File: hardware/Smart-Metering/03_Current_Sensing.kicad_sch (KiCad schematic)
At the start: 40 parts, among them J301 SENSOR_IA, J302 SENSOR_IB, J303 SENSOR_IC, J304 SENSOR_IN

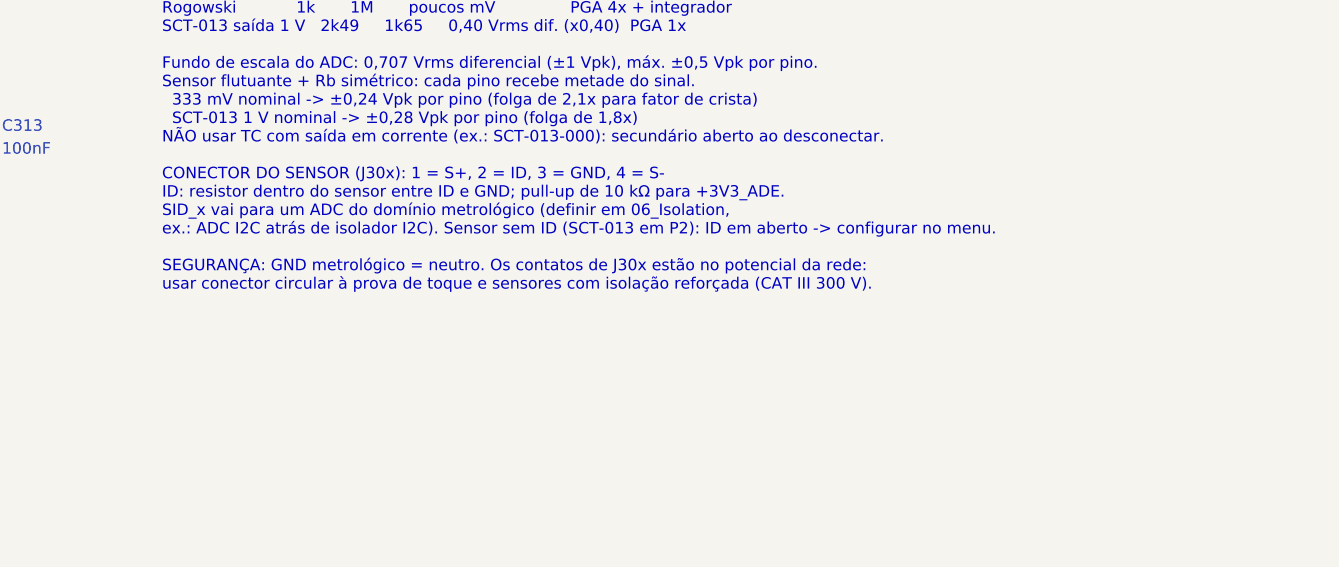
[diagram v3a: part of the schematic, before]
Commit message: Resolve as pendências da revisão do esquemático
P1  ADE9430: footprint VQFN-40 6x6 com EP de 4,15 mm, compatível com as
    variantes CP-40 de 6x6 mm (EP de 3,9 a 4,7 mm).
P2  Confirmado no datasheet: MISO solto com SS alto (pull-up de 100 kΩ)
    e NC1/NC2 em GND, como já estava.
P3  J301-J304: headers JST PH de 4 vias cabeados até conectores M8
    fêmea de painel (à prova de toque).
P4  PS601 -> U606 ADuM6000 (isoPower 5 kVrms, símbolo oficial).
P5  PS101 -> RAC20-05SK/277 (85-305 VAC, 120-430 VDC, 20 W); fusíveis
    T500mA, R101 3 W, C101 10 uF/450 V; entrada do BQ25895 a 3 A.
P7  TPS61089 -> TPS61022 (compensação interna, sem valores a ajustar).
P8  Placa EV alimentada pelos pinos 5 V do J1 (nota na folha 07).
P9  EEPROM de calibração 24LC64 no I2C1.
P10 Labels globais de uma só folha convertidos em locais.

Verificação: 223 componentes, nenhum pino solto, nenhuma net sem fonte,
nenhum conflito de saída, isolação íntegra, todos os footprints
existentes na biblioteca oficial do KiCad.

Co-Authored-By: Claude Opus 5.5 <noreply@anthropic.com>
Claude-Session: https://claude.ai/code/session_012B8cVkhtjf3eg98UdpNCpf
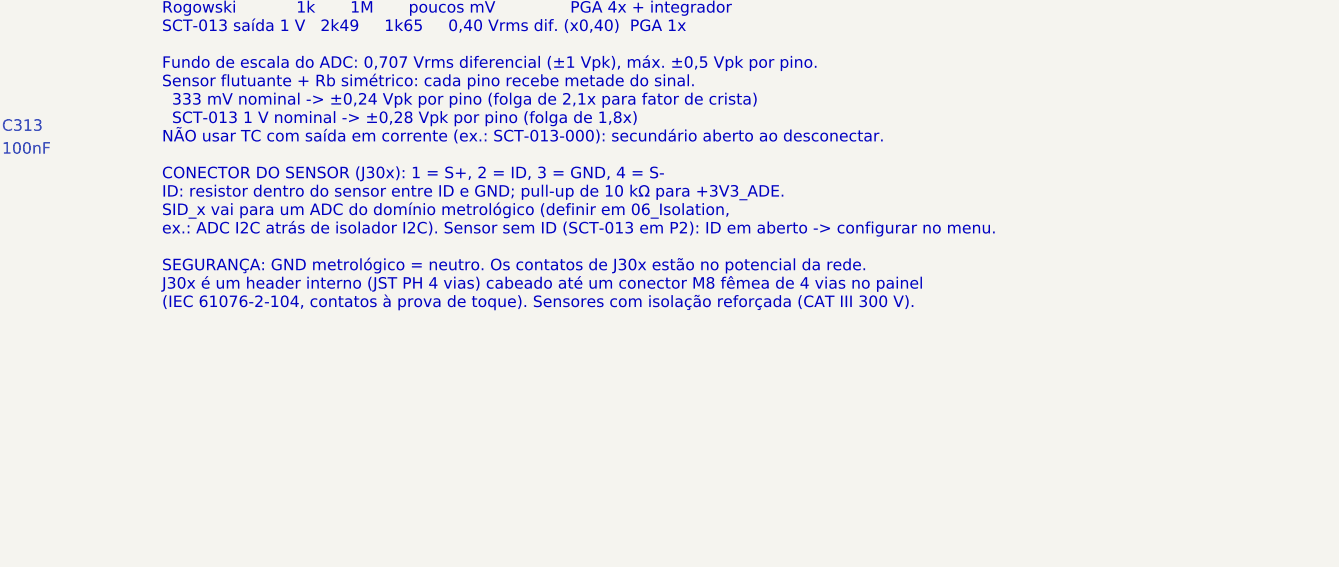
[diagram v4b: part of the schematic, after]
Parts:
- J301, J302, J303, J304: footprint (none) -> Connector_JST:JST_PH_B4B-PH-K_1x04_P2.00mm_Vertical
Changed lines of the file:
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@@
 		(comment 2 "Per leg: Ra series + Rb to GND + 22 nF; Thevenin kept at 1 kOhm for 7.2 kHz anti-aliasing")
 	)
-	(text "FRONT-END DE CORRENTE — ENTRADA CONFIGURÁVEL POR MONTAGEM\n\nPor perna: sensor -> Ra (série) -> nó -> Rb para GND + 22 nF -> IxP / IxN\nRa // Rb = 1 kΩ em todas as opções -> fc ≈ 7,2 kHz (igual aos canais de tensão)\n\nOPÇÃO               Ra       Rb       sinal nominal no ADC    ADE9430\nTC 333 mV (padrão)  1k       1M       0,333 Vrms dif.         PGA 1x\nRogowski            1k       1M       poucos mV               PGA 4x + integrador\nSCT-013 saída 1 V   2k49     1k65     0,40 Vrms dif. (x0,40)  PGA 1x\n\nFundo de escala do ADC: 0,707 Vrms diferencial (±1 Vpk), máx. ±0,5 Vpk por pino.\nSensor flutuante + Rb simétrico: cada pino recebe metade do sinal.\n  333 mV nominal -> ±0,24 Vpk por pino (folga de 2,1x para fator de crista)\n  SCT-013 1 V nominal -> ±0,28 Vpk por pino (folga de 1,8x)\nNÃO usar TC com saída em corrente (ex.: SCT-013-000): secundário aberto ao desconectar.\n\nCONECTOR DO SENSOR (J30x): 1 = S+, 2 = ID, 3 = GND, 4 = S-\nID: resistor dentro do sensor entre ID e GND; pull-up de 10 kΩ para +3V3_ADE.\nSID_x vai para um ADC do domínio metrológico (definir em 06_Isolation,\nex.: ADC I2C atrás de isolador I2C). Sensor sem ID (SCT-013 em P2): ID em aberto -> configurar no menu.\n\nSEGURANÇA: GND metrológico = neutro. Os contatos de J30x estão no potencial da rede:\nusar conector circular à prova de toque e sensores com isolação reforçada (CAT III 300 V)."
+	(text "FRONT-END DE CORRENTE — ENTRADA CONFIGURÁVEL POR MONTAGEM\n\nPor perna: sensor -> Ra (série) -> nó -> Rb para GND + 22 nF -> IxP / IxN\nRa // Rb = 1 kΩ em todas as opções -> fc ≈ 7,2 kHz (igual aos canais de tensão)\n\nOPÇÃO               Ra       Rb       sinal nominal no ADC    ADE9430\nTC 333 mV (padrão)  1k       1M       0,333 Vrms dif.         PGA 1x\nRogowski            1k       1M       poucos mV               PGA 4x + integrador\nSCT-013 saída 1 V   2k49     1k65     0,40 Vrms dif. (x0,40)  PGA 1x\n\nFundo de escala do ADC: 0,707 Vrms diferencial (±1 Vpk), máx. ±0,5 Vpk por pino.\nSensor flutuante + Rb simétrico: cada pino recebe metade do sinal.\n  333 mV nominal -> ±0,24 Vpk por pino (folga de 2,1x para fator de crista)\n  SCT-013 1 V nominal -> ±0,28 Vpk por pino (folga de 1,8x)\nNÃO usar TC com saída em corrente (ex.: SCT-013-000): secundário aberto ao desconectar.\n\nCONECTOR DO SENSOR (J30x): 1 = S+, 2 = ID, 3 = GND, 4 = S-\nID: resistor dentro do sensor entre ID e GND; pull-up de 10 kΩ para +3V3_ADE.\nSID_x vai para um ADC do domínio metrológico (definir em 06_Isolation,\nex.: ADC I2C atrás de isolador I2C). Sensor sem ID (SCT-013 em P2): ID em aberto -> configurar no menu.\n\nSEGURANÇA: GND metrológico = neutro. Os contatos de J30x estão no potencial da rede.\nJ30x é um header interno (JST PH 4 vias) cabeado até um conector M8 fêmea de 4 vias no painel\n(IEC 61076-2-104, contatos à prova de toque). Sensores com isolação reforçada (CAT III 300 V)."
 		(exclude_from_sim no)(at 154.94 25.4 0)
 		(effects (font (size 1.27 1.27)) (justify left top))
@@
 		(property "Reference" "J301" (at 25.4 44.45 0) (effects (font (size 1.27 1.27))))
 		(property "Value" "SENSOR_IA" (at 25.4 57.15 0) (effects (font (size 1.27 1.27))))
-		(property "Footprint" "" (at 25.4 50.8 0) (effects (font (size 1.27 1.27)) (hide yes)))
+		(property "Footprint" "Connector_JST:JST_PH_B4B-PH-K_1x04_P2.00mm_Vertical" (at 25.4 50.8 0) (effects (font (size 1.27 1.27)) (hide yes)))
 		(property "Datasheet" "" (at 25.4 50.8 0) (effects (font (size 1.27 1.27)) (hide yes)))
-		(property "Description" "Current sensor connector, phase A: 1=S+ 2=ID 3=GND 4=S-; touch-safe circular, footprint TBD" (at 25.4 50.8 0) (effects (font (size 1.27 1.27)) (hide yes)))
+		(property "Description" "Internal header to panel M8 4-pin female (touch-safe) for phase A: 1=S+ 2=ID 3=GND 4=S-" (at 25.4 50.8 0) (effects (font (size 1.27 1.27)) (hide yes)))
 		(pin "1")
 		(pin "2")
@@
 		(property "Reference" "J302" (at 25.4 95.25 0) (effects (font (size 1.27 1.27))))
 		(property "Value" "SENSOR_IB" (at 25.4 107.95 0) (effects (font (size 1.27 1.27))))
-		(property "Footprint" "" (at 25.4 101.6 0) (effects (font (size 1.27 1.27)) (hide yes)))
+		(property "Footprint" "Connector_JST:JST_PH_B4B-PH-K_1x04_P2.00mm_Vertical" (at 25.4 101.6 0) (effects (font (size 1.27 1.27)) (hide yes)))
 		(property "Datasheet" "" (at 25.4 101.6 0) (effects (font (size 1.27 1.27)) (hide yes)))
-		(property "Description" "Current sensor connector, phase B: 1=S+ 2=ID 3=GND 4=S-; touch-safe circular, footprint TBD" (at 25.4 101.6 0) (effects (font (size 1.27 1.27)) (hide yes)))
+		(property "Description" "Internal header to panel M8 4-pin female (touch-safe) for phase B: 1=S+ 2=ID 3=GND 4=S-" (at 25.4 101.6 0) (effects (font (size 1.27 1.27)) (hide yes)))
 		(pin "1")
 		(pin "2")
@@
 		(property "Reference" "J303" (at 25.4 146.05 0) (effects (font (size 1.27 1.27))))
 		(property "Value" "SENSOR_IC" (at 25.4 158.75 0) (effects (font (size 1.27 1.27))))
-		(property "Footprint" "" (at 25.4 152.4 0) (effects (font (size 1.27 1.27)) (hide yes)))
+		(property "Footprint" "Connector_JST:JST_PH_B4B-PH-K_1x04_P2.00mm_Vertical" (at 25.4 152.4 0) (effects (font (size 1.27 1.27)) (hide yes)))
 		(property "Datasheet" "" (at 25.4 152.4 0) (effects (font (size 1.27 1.27)) (hide yes)))
-		(property "Description" "Current sensor connector, phase C: 1=S+ 2=ID 3=GND 4=S-; touch-safe circular, footprint TBD" (at 25.4 152.4 0) (effects (font (size 1.27 1.27)) (hide yes)))
+		(property "Description" "Internal header to panel M8 4-pin female (touch-safe) for phase C: 1=S+ 2=ID 3=GND 4=S-" (at 25.4 152.4 0) (effects (font (size 1.27 1.27)) (hide yes)))
 		(pin "1")
 		(pin "2")
@@
 		(property "Reference" "J304" (at 25.4 196.85 0) (effects (font (size 1.27 1.27))))
 		(property "Value" "SENSOR_IN" (at 25.4 209.55 0) (effects (font (size 1.27 1.27))))
-		(property "Footprint" "" (at 25.4 203.2 0) (effects (font (size 1.27 1.27)) (hide yes)))
+		(property "Footprint" "Connector_JST:JST_PH_B4B-PH-K_1x04_P2.00mm_Vertical" (at 25.4 203.2 0) (effects (font (size 1.27 1.27)) (hide yes)))
 		(property "Datasheet" "" (at 25.4 203.2 0) (effects (font (size 1.27 1.27)) (hide yes)))
-		(property "Description" "Current sensor connector, neutral: 1=S+ 2=ID 3=GND 4=S-; touch-safe circular, footprint TBD" (at 25.4 203.2 0) (effects (font (size 1.27 1.27)) (hide yes)))
-		(pin "1")
-		(pin "2")
+		(property "Description" "Internal header to panel M8 4-pin female (touch-safe) for neutral: 1=S+ 2=ID 3=GND 4=S-" (at 25.4 203.2 0) (effects (font (size 1.27 1.27)) (hide yes)))
+		(pin "1")
+		(pin "2")
